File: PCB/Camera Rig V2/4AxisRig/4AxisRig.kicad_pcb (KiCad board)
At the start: 2 copper layers, 77 parts, among them J1 Conn_01x04_Socket, J2 SJ-3524-SMT, J3 Motor Connector, J4 Motor Connector, J5 USB_C_Receptacle_USB2.0_14P, J6 Motor Connector, Q1 NMOS, Q2 NMOS, U1 TPS25730DREFR, U4 ESP32-S3-WROOM-1, U5 TMC2209-LA, U6 TMC2209-LA, U7 TMC2209-LA

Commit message: PCB V2 first draft
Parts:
- added C1: 10uF, Capacitor_SMD:C_0603_1608Metric_Pad1.08x0.95mm_HandSolder, F.Cu at (131.9, 79.6)
- added C10: 10uF, Capacitor_SMD:C_0603_1608Metric_Pad1.08x0.95mm_HandSolder, F.Cu at (136.0, 67.7)
- added C11: 0.01uF, Capacitor_SMD:C_0603_1608Metric_Pad1.08x0.95mm_HandSolder, F.Cu at (132.8, 67.7)
- added C12: 330pF, Capacitor_SMD:C_0603_1608Metric_Pad1.08x0.95mm_HandSolder, F.Cu at (130.7, 73.0)
- added C13: 330pF, Capacitor_SMD:C_0603_1608Metric_Pad1.08x0.95mm_HandSolder, F.Cu at (130.7, 71.4)
- added C14: 10uF, Capacitor_SMD:C_0603_1608Metric_Pad1.08x0.95mm_HandSolder, F.Cu at (168.0, 76.1)
- added C15: 100nF, Capacitor_SMD:C_0603_1608Metric_Pad1.08x0.95mm_HandSolder, F.Cu at (164.3, 72.7)
- added C16: 47pF, Capacitor_SMD:C_0603_1608Metric_Pad1.08x0.95mm_HandSolder, F.Cu at (163.0, 80.5)
- added C17: 22uF, Capacitor_SMD:C_1206_3216Metric_Pad1.33x1.80mm_HandSolder, F.Cu at (159.2, 76.3)
- added C18: 22uF, Capacitor_SMD:C_1206_3216Metric_Pad1.33x1.80mm_HandSolder, F.Cu at (161.7, 76.3)
- added C19: 10uF, Capacitor_SMD:C_0603_1608Metric_Pad1.08x0.95mm_HandSolder, F.Cu at (155.4, 76.3)
- added C2: 10uF, Capacitor_SMD:C_0603_1608Metric_Pad1.08x0.95mm_HandSolder, F.Cu at (134.1, 78.6)
- added C20: 100nF, Capacitor_SMD:C_0603_1608Metric_Pad1.08x0.95mm_HandSolder, F.Cu at (151.9, 72.7)
- added C21: 47pF, Capacitor_SMD:C_0603_1608Metric_Pad1.08x0.95mm_HandSolder, F.Cu at (150.4, 80.6)
- added C22: 22uF, Capacitor_SMD:C_1206_3216Metric_Pad1.33x1.80mm_HandSolder, F.Cu at (149.1, 76.4)
- added C23: 22uF, Capacitor_SMD:C_1206_3216Metric_Pad1.33x1.80mm_HandSolder, F.Cu at (146.5, 76.4)
- added C24: 22uF, Capacitor_SMD:C_1206_3216Metric_Pad1.33x1.80mm_HandSolder, F.Cu at (85.4, 96.5)
- added C25: 1uF, Capacitor_SMD:C_0603_1608Metric_Pad1.08x0.95mm_HandSolder, F.Cu at (88.8, 97.0)
- added C26: 100nF, Capacitor_SMD:C_0603_1608Metric_Pad1.08x0.95mm_HandSolder, F.Cu at (84.6, 94.5)
- added C27: 100nF, Capacitor_SMD:C_0603_1608Metric_Pad1.08x0.95mm_HandSolder, F.Cu at (101.3, 64.6)
- added C28: 100nF, Capacitor_SMD:C_0603_1608Metric_Pad1.08x0.95mm_HandSolder, F.Cu at (88.8, 101.8)
- added C29: 100nF 16V, Capacitor_SMD:C_0603_1608Metric_Pad1.08x0.95mm_HandSolder, F.Cu at (167.0, 93.4)
- added C3: 4.7uF, Capacitor_SMD:C_0603_1608Metric_Pad1.08x0.95mm_HandSolder, F.Cu at (136.4, 78.6)
- added C30: 22nF 50V, Capacitor_SMD:C_0603_1608Metric_Pad1.08x0.95mm_HandSolder, F.Cu at (167.5, 95.0)
- added C31: 2.2uF 6.3V, Capacitor_SMD:C_0603_1608Metric_Pad1.08x0.95mm_HandSolder, F.Cu at (164.7, 90.5)
- added C32: 100nF, Capacitor_SMD:C_0603_1608Metric_Pad1.08x0.95mm_HandSolder, F.Cu at (165.5, 98.6)
- added C33: 100nF, Capacitor_SMD:C_0603_1608Metric_Pad1.08x0.95mm_HandSolder, F.Cu at (158.5, 98.6)
- added C34: 100uF, 865080545012:WCAP-ASLI_6.3X7.7_DXL_, F.Cu at (171.7, 89.4)
- added C35: 100nF, Capacitor_SMD:C_0603_1608Metric_Pad1.08x0.95mm_HandSolder, F.Cu at (156.9, 108.0)
- added C36: 100nF, Capacitor_SMD:C_0603_1608Metric_Pad1.08x0.95mm_HandSolder, F.Cu at (160.4, 108.0)
- added C37: 100nF, Capacitor_SMD:C_0603_1608Metric_Pad1.08x0.95mm_HandSolder, F.Cu at (164.0, 108.1)
- added C38: 100nF, Capacitor_SMD:C_0603_1608Metric_Pad1.08x0.95mm_HandSolder, F.Cu at (167.6, 108.1)
- added C39: 100nF 16V, Capacitor_SMD:C_0603_1608Metric_Pad1.08x0.95mm_HandSolder, F.Cu at (150.0, 93.3)
- added C4: 4.7uF, Capacitor_SMD:C_0603_1608Metric_Pad1.08x0.95mm_HandSolder, F.Cu at (131.2, 67.7)
- added C40: 22nF 50V, Capacitor_SMD:C_0603_1608Metric_Pad1.08x0.95mm_HandSolder, F.Cu at (150.5, 94.9)
- added C41: 2.2uF 6.3V, Capacitor_SMD:C_0603_1608Metric_Pad1.08x0.95mm_HandSolder, F.Cu at (147.7, 90.5)
- added C42: 100nF, Capacitor_SMD:C_0603_1608Metric_Pad1.08x0.95mm_HandSolder, F.Cu at (148.5, 98.6)
- added C43: 100nF, Capacitor_SMD:C_0603_1608Metric_Pad1.08x0.95mm_HandSolder, F.Cu at (141.5, 98.6)
- added C44: 100uF, 865080545012:WCAP-ASLI_6.3X7.7_DXL_, F.Cu at (154.7, 89.4)
- added C45: 100nF, Capacitor_SMD:C_0603_1608Metric_Pad1.08x0.95mm_HandSolder, F.Cu at (139.9, 108.0)
- added C46: 100nF, Capacitor_SMD:C_0603_1608Metric_Pad1.08x0.95mm_HandSolder, F.Cu at (143.4, 108.0)
- added C47: 100nF, Capacitor_SMD:C_0603_1608Metric_Pad1.08x0.95mm_HandSolder, F.Cu at (147.0, 108.0)
- added C48: 100nF, Capacitor_SMD:C_0603_1608Metric_Pad1.08x0.95mm_HandSolder, F.Cu at (150.6, 108.0)
- added C49: 100nF 16V, Capacitor_SMD:C_0603_1608Metric_Pad1.08x0.95mm_HandSolder, F.Cu at (133.0, 93.3)
- added C5: 0.01uF, Capacitor_SMD:C_0603_1608Metric_Pad1.08x0.95mm_HandSolder, F.Cu at (130.7, 76.2)
- added C50: 22nF 50V, Capacitor_SMD:C_0603_1608Metric_Pad1.08x0.95mm_HandSolder, F.Cu at (133.5, 94.9)
- added C51: 2.2uF 6.3V, Capacitor_SMD:C_0603_1608Metric_Pad1.08x0.95mm_HandSolder, F.Cu at (130.7, 90.5)
- added C52: 100nF, Capacitor_SMD:C_0603_1608Metric_Pad1.08x0.95mm_HandSolder, F.Cu at (131.5, 98.6)
- added C53: 100nF, Capacitor_SMD:C_0603_1608Metric_Pad1.08x0.95mm_HandSolder, F.Cu at (124.5, 98.6)
- added C54: 100uF, 865080545012:WCAP-ASLI_6.3X7.7_DXL_, F.Cu at (137.7, 89.5)
- added C55: 100nF, Capacitor_SMD:C_0603_1608Metric_Pad1.08x0.95mm_HandSolder, F.Cu at (122.5, 108.0)
- added C56: 100nF, Capacitor_SMD:C_0603_1608Metric_Pad1.08x0.95mm_HandSolder, F.Cu at (126.4, 108.0)
- added C57: 100nF, Capacitor_SMD:C_0603_1608Metric_Pad1.08x0.95mm_HandSolder, F.Cu at (130.0, 108.0)
- added C58: 100nF, Capacitor_SMD:C_0603_1608Metric_Pad1.08x0.95mm_HandSolder, F.Cu at (133.6, 108.0)
- added C6: 0.01uF, Capacitor_SMD:C_0603_1608Metric_Pad1.08x0.95mm_HandSolder, F.Cu at (130.7, 74.6)
- added C7: 22uF, Capacitor_SMD:C_1206_3216Metric_Pad1.33x1.80mm_HandSolder, F.Cu at (138.1, 66.9)
- added C8: 22uF, Capacitor_SMD:C_1206_3216Metric_Pad1.33x1.80mm_HandSolder, F.Cu at (140.7, 66.9)
- added C9: 0.01uF, Capacitor_SMD:C_0603_1608Metric_Pad1.08x0.95mm_HandSolder, F.Cu at (134.4, 67.7)
- added D1: ESD441, Diode_SMD:D_0402_1005Metric_Pad0.77x0.64mm_HandSolder, F.Cu at (115.9, 72.0)
- added D2: ESD441, Diode_SMD:D_0402_1005Metric_Pad0.77x0.64mm_HandSolder, F.Cu at (118.1, 72.0)
- added D3: ESD441, Diode_SMD:D_0402_1005Metric_Pad0.77x0.64mm_HandSolder, F.Cu at (119.4, 72.0)
- added D4: ESD441, Diode_SMD:D_0402_1005Metric_Pad0.77x0.64mm_HandSolder, F.Cu at (114.7, 72.0)
- added D5: SMAJ10CA-13-F, SMAJ10CA-13-F:SMA_DIO, F.Cu at (124.0, 70.2)
- added FB13: 2512065007Y6, Inductor_SMD:L_1206_3216Metric_Pad1.22x1.90mm_HandSolder, F.Cu at (85.4, 99.0)
- added H1: MountingHole, MountingHole:MountingHole_3.2mm_M3, F.Cu at (173.0, 66.0)
- added H2: MountingHole, MountingHole:MountingHole_3.2mm_M3, F.Cu at (173.0, 113.0)
- added H3: MountingHole, MountingHole:MountingHole_3.2mm_M3, F.Cu at (86.0, 66.0)
- added H4: MountingHole, MountingHole:MountingHole_3.2mm_M3, F.Cu at (86.0, 113.0)
- added L1: 4.7uH, DR74-4R7-R:DR74, F.Cu at (160.4, 67.5)
- added L2: 15uH, DR74-150-R:DR74, F.Cu at (149.4, 67.6)
- added R45: 4.7k, Resistor_SMD:R_0603_1608Metric_Pad0.98x0.95mm_HandSolder, F.Cu at (88.3, 70.4)
- added R46: 10k, Resistor_SMD:R_0603_1608Metric_Pad0.98x0.95mm_HandSolder, F.Cu at (90.5, 101.8)
- added SW1: PTS810SJS250SMTRLFS, PTS810SJS250SMTR:SMT_MTRLFS_CNK, F.Cu at (105.7, 64.5)
- added SW2: SW_SPDT, SS-12D07-VG 4 NS GA PA:SS12D07_CNK, F.Cu at (107.8, 69.6)
- added SW3: PEC11L-4120F-S0020, PEC11L-4120F-S0020:PEC11L-4x20F-Sxxx_BRN, F.Cu at (101.9, 100.4)
- added TP1: TestPoint, TestPoint:TestPoint_Pad_2.0x2.0mm, F.Cu at (131.5, 83.5)
- FB1, FB10, FB11, FB12, FB2, FB3, FB4, FB5, FB6, FB7, FB8, FB9: value 50@100MHz -> 2512065007Y6
- J1: value Conn_01x04_Socket -> Conn_01x05_Socket
- J5: value USB_C_Receptacle_USB2.0_14P -> USB_C_Receptacle_USB2.0_16P; footprint USB_GCT:CONN_8p94X6p5X3p16_12L_GCC -> USB_C_Receptacle_USB2.0_14P:CONN_8p94X6p5X3p16_12L_GCC
- Q1, Q2: footprint 2N7002KT7G:SOT95P240X111-3N -> 2N7000:SOT95P240X111-3N
- R19: value 10k -> 100k
- R20: value 10k -> 25k
- R21, R22: value 500 -> 10k
- R27, R33, R41: value 220m -> 10k
- R28, R34, R42: value 220m -> 0.68; footprint Resistor_SMD:R_0603_1608Metric_Pad0.98x0.95mm_HandSolder -> Resistor_SMD:R_1206_3216Metric_Pad1.30x1.75mm_HandSolder
- R29: value 10k -> 0.68; footprint Resistor_SMD:R_0603_1608Metric_Pad0.98x0.95mm_HandSolder -> Resistor_SMD:R_1206_3216Metric_Pad1.30x1.75mm_HandSolder
- R35: value 5.1k -> 0.68; footprint Resistor_SMD:R_0603_1608Metric_Pad0.98x0.95mm_HandSolder -> Resistor_SMD:R_1206_3216Metric_Pad1.30x1.75mm_HandSolder
- R36: value 5.1k -> 5.1k+-10%
- R37: value 10k -> 5.1k+-10%
- R43: value 100k -> 0.68; footprint Resistor_SMD:R_0603_1608Metric_Pad0.98x0.95mm_HandSolder -> Resistor_SMD:R_1206_3216Metric_Pad1.30x1.75mm_HandSolder
- R44: value 25k -> 4.7k
- RV1, RV2, RV3, RV4, RV5, RV6: footprint Resistor_SMD:R_0603_1608Metric_Pad0.98x0.95mm_HandSolder -> Resistor_SMD:R_1206_3216Metric_Pad1.30x1.75mm_HandSolder
- U2, U3: value ~ -> AN_SY8105
- moved J1 104.7 mm to (94.4, 65.5)
- moved R1 91.4 mm to (95.5, 94.4)
- moved J5 74.9 mm to (117.0, 64.9), turned to 180 degrees
- moved R36 69.2 mm to (120.7, 72.5), turned to -90 degrees
- moved J4 61.5 mm to (149.0, 113.5), turned to -90 degrees
- moved FB5 55.0 mm to (141.3, 104.5), turned to -90 degrees
- moved J6 53.6 mm to (132.0, 113.5), turned to -90 degrees
- moved FB6 50.7 mm to (143.9, 104.5), turned to -90 degrees
- moved FB9 50.6 mm to (124.3, 104.5), turned to -90 degrees
- moved U1 50.4 mm to (135.2, 73.2), turned to 90 degrees
- moved R34 49.7 mm to (124.6, 100.6)
- moved R29 49.4 mm to (141.6, 100.6)
- moved R37 49.3 mm to (113.4, 72.5), turned to -90 degrees
- moved R5 49.2 mm to (128.0, 72.4), turned to -90 degrees
- moved FB10 46.7 mm to (126.9, 104.5), turned to -90 degrees
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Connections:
- net /D+ renamed /USB_D+
- net /D- renamed /USB_D-
- FB1 pad 1: /TMC2209 1/OA1 -> /TMC2209 1/OA2
- FB10 pad 1: /TMC2209 3/OA2 -> /TMC2209 3/OA1
- FB2 pad 1: /TMC2209 1/OA2 -> /TMC2209 1/OA1
- FB5 pad 1: /TMC2209 2/OA1 -> /TMC2209 2/OA2
- FB6 pad 1: /TMC2209 2/OA2 -> /TMC2209 2/OA1
- FB9 pad 1: /TMC2209 3/OA1 -> /TMC2209 3/OA2
- J1 pad MP: (no net) -> unconnected-(J1-Pin_5-PadMP)_1
- J5 pad A5: /USB Power/CC1 -> /USB_CC1
- J5 pad A8: (no net) -> unconnected-(J5-SBU1-PadA8)
- J5 pad B5: /USB Power/CC2 -> /USB_CC2
- J5 pad B8: (no net) -> unconnected-(J5-SBU2-PadB8)
- R19 pad 1: /EN -> Net-(U4-IO41)
- R19 pad 2: +3V3 -> /PPHV
- R20 pad 1: /MCU ESP32/BOOT -> GND
- R20 pad 2: +3V3 -> Net-(U4-IO41)
- R21 pad 1: /SHUTTER -> /MCU ESP32/EN
- R21 pad 2: Net-(Q1-G) -> +3V3
- R22 pad 1: /FOCUS -> /SHUTTER
- R22 pad 2: Net-(Q2-G) -> Net-(Q1-G)
- R23 pad 1: GND -> /FOCUS
- R23 pad 2: /TMC2209 1/AD0 -> Net-(Q2-G)
- R24 pad 1: /TMC2209 1/AD0 -> GND
- R24 pad 2: +3V3 -> /TMC2209 1/AD0
- R25 pad 1: GND -> /TMC2209 1/AD0
- R25 pad 2: /TMC2209 1/AD1 -> +3V3
- R26 pad 1: /TMC2209 1/AD1 -> GND
- R26 pad 2: +3V3 -> /TMC2209 1/AD1
- R27 pad 1: GND -> /TMC2209 1/AD1
- R27 pad 2: Net-(U5-BRB) -> +3V3
- R29 pad 2: /TMC2209 2/AD0 -> Net-(U6-BRA)
- R30 pad 1: /TMC2209 2/AD0 -> GND
- R30 pad 2: +3V3 -> /TMC2209 2/AD0
- R31 pad 1: GND -> /TMC2209 2/AD0
- R31 pad 2: /TMC2209 2/AD1 -> +3V3
- R32 pad 1: /TMC2209 2/AD1 -> GND
- R32 pad 2: +3V3 -> /TMC2209 2/AD1
- R33 pad 1: GND -> /TMC2209 2/AD1
- R33 pad 2: Net-(U6-BRB) -> +3V3
- R34 pad 2: Net-(U6-BRA) -> Net-(U7-BRA)
- R35 pad 1: /USB Power/CC1 -> GND
- R35 pad 2: GND -> Net-(U5-BRB)
- R36 pad 1: /USB Power/CC2 -> /USB_CC1
- R37 pad 1: GND -> /USB_CC2
- R37 pad 2: /TMC2209 3/AD0 -> GND
- R38 pad 1: /TMC2209 3/AD0 -> GND
- R38 pad 2: +3V3 -> /TMC2209 3/AD0
- R39 pad 1: GND -> /TMC2209 3/AD0
- R39 pad 2: /TMC2209 3/AD1 -> +3V3
- R40 pad 1: /TMC2209 3/AD1 -> GND
- R40 pad 2: +3V3 -> /TMC2209 3/AD1
- R41 pad 1: GND -> /TMC2209 3/AD1
- R41 pad 2: Net-(U7-BRB) -> +3V3
- R42 pad 2: Net-(U7-BRA) -> Net-(U6-BRB)
- R43 pad 1: Net-(U4-IO3) -> GND
- R43 pad 2: /PPHV -> Net-(U7-BRB)
- R44 pad 1: GND -> /I2C_SCL
- R44 pad 2: Net-(U4-IO3) -> +3V3
- U1 pad 20: /Buck Converter 12V/VIN -> /PPHV
- U1 pad 21: /Buck Converter 12V/VIN -> /PPHV
- U1 pad 22: /Buck Converter 12V/VIN -> /PPHV
- U1 pad 28: /USB Power/CC1 -> /USB_CC1
- U1 pad 29: /USB Power/CC2 -> /USB_CC2
- U2 pad 4: /Buck Converter 12V/VIN -> /PPHV
- U3 pad 4: /Buck Converter 12V/VIN -> /PPHV
- U4 pad 12: /STEP2 -> unconnected-(U4-IO8-Pad12)
- U4 pad 15: Net-(U4-IO3) -> /SPREAD
- U4 pad 16: /ENC_C -> /EN_DRIVERS
- U4 pad 17: /DIR2 -> /STDBY3
- U4 pad 18: /DIAG2 -> /DIR3
- U4 pad 19: /STDBY2 -> /STEP3
- U4 pad 2: +3V3 -> Net-(U4-3V3)
- U4 pad 20: /STEP3 -> /DIAG3
- U4 pad 21: /DIR3 -> /STDBY2
- U4 pad 22: /DIAG3 -> /DIR2
- U4 pad 23: unconnected-(U4-IO21-Pad23) -> /STEP2
- U4 pad 24: /ENC_B -> /DIAG2
- U4 pad 25: /SPREAD -> /STDBY1
- U4 pad 26: /ENC_A -> /DIR1
- U4 pad 28: unconnected-(U4-IO35-Pad28) -> /STEP1
- U4 pad 29: unconnected-(U4-IO36-Pad29) -> /DIAG1
- U4 pad 3: /EN -> /MCU ESP32/EN
- U4 pad 32: /EN_12V -> unconnected-(U4-IO39-Pad32)
- U4 pad 33: /SW -> /EN_12V
- U4 pad 34: /SHUTTER -> Net-(U4-IO41)
- U4 pad 35: /FOCUS -> unconnected-(U4-IO42-Pad35)
- U4 pad 4: /STEP1 -> /SW
- U4 pad 5: /DIR1 -> /ENC_B
- U4 pad 6: /DIAG1 -> /ENC_C
- U4 pad 7: /STDBY1 -> /ENC_A
- U4 pad 8: /STDBY3 -> /SHUTTER
- U4 pad 9: /EN -> /FOCUS
- U5 pad 2: /EN -> /EN_DRIVERS
- U6 pad 2: /EN -> /EN_DRIVERS
- U7 pad 2: /EN -> /EN_DRIVERS
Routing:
- net /SPREAD: track 0.00 -> 171.6 mm, vias 0 -> 4
- net GND: track 0.00 -> 156.0 mm, vias 0 -> 95
- net /EN_DRIVERS: track 0.00 -> 154.9 mm, vias 0 -> 4
- net /UART_TX/RX: track 0.00 -> 87.4 mm, vias 0 -> 4
- net /EN_12V: track 0.00 -> 83.0 mm, vias 0 -> 4
- net /DIAG1: track 0.00 -> 73.6 mm, vias 0 -> 2
- net /STEP1: track 0.00 -> 69.7 mm, vias 0 -> 2
- net /DIR1: track 0.00 -> 65.9 mm, vias 0 -> 2
- net /STDBY1: track 0.00 -> 65.6 mm, vias 0 -> 2
- net +3V3: track 0.00 -> 57.8 mm, vias 0 -> 24
- net /PPHV: track 0.00 -> 55.8 mm, vias 0 -> 36
- net /USB_D-: track 0.00 -> 52.0 mm
- net /USB_D+: track 0.00 -> 49.9 mm
- net /DIAG2: track 0.00 -> 49.5 mm, vias 0 -> 2
- net /MCU ESP32/EN: track 0.00 -> 48.4 mm, vias 0 -> 2
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- added copper zone on F.Cu, net +12V
- added copper zone on In2.Cu, net +12V
- added copper zone on F.Cu, net +3V3
- added copper zone on In2.Cu, net +3V3
- added copper zone on F.Cu, net /PPHV
- added copper zone on In2.Cu, net /PPHV
- added copper zone on F.Cu, net /USB Power/VBUS
- added copper zone on In2.Cu, net /USB Power/VBUS
- added copper zone on B.Cu, net GND
- added copper zone on F.Cu, net GND
- added copper zone on In1.Cu, net GND
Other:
- board outline added: 95 x 55 mm
- copper layers 2 -> 4
- board text added: "Camera Motion Driver V2 Andrew Josephbek"

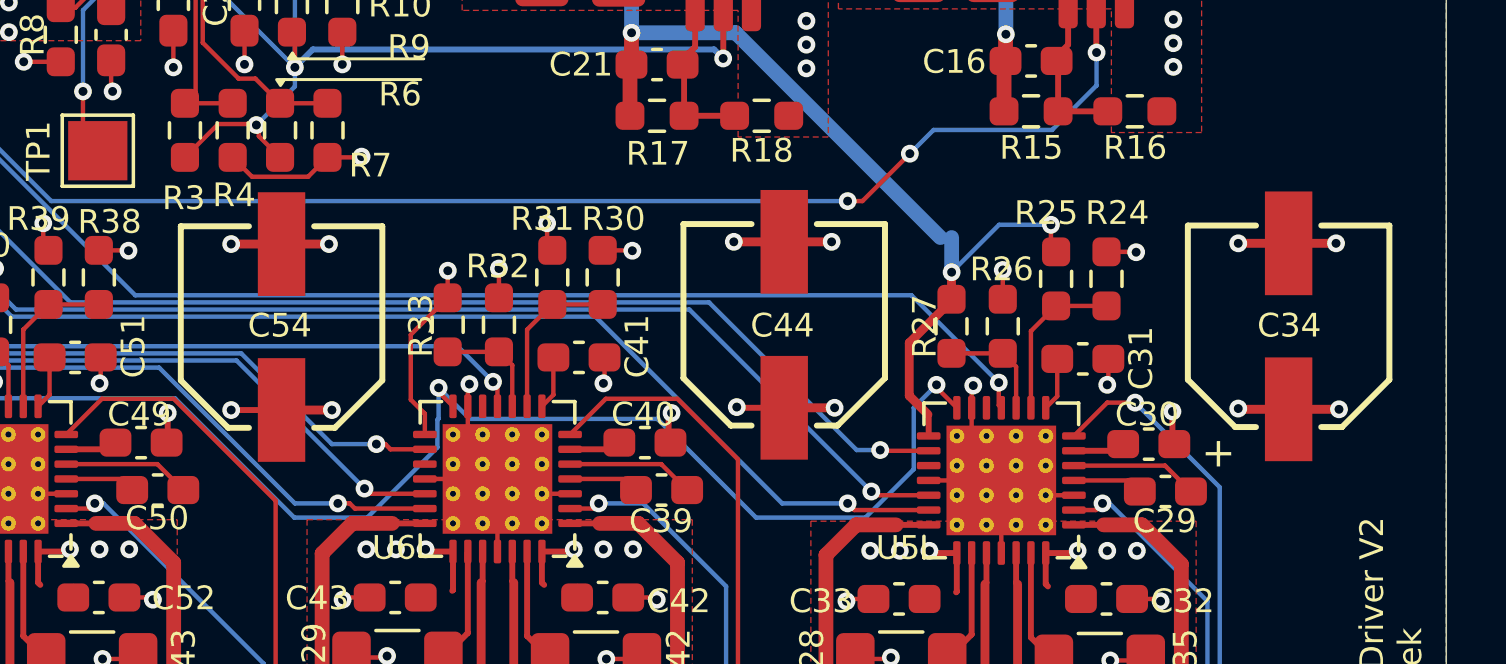
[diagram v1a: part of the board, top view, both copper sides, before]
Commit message: REplaced bulk caps w low esr ceramics
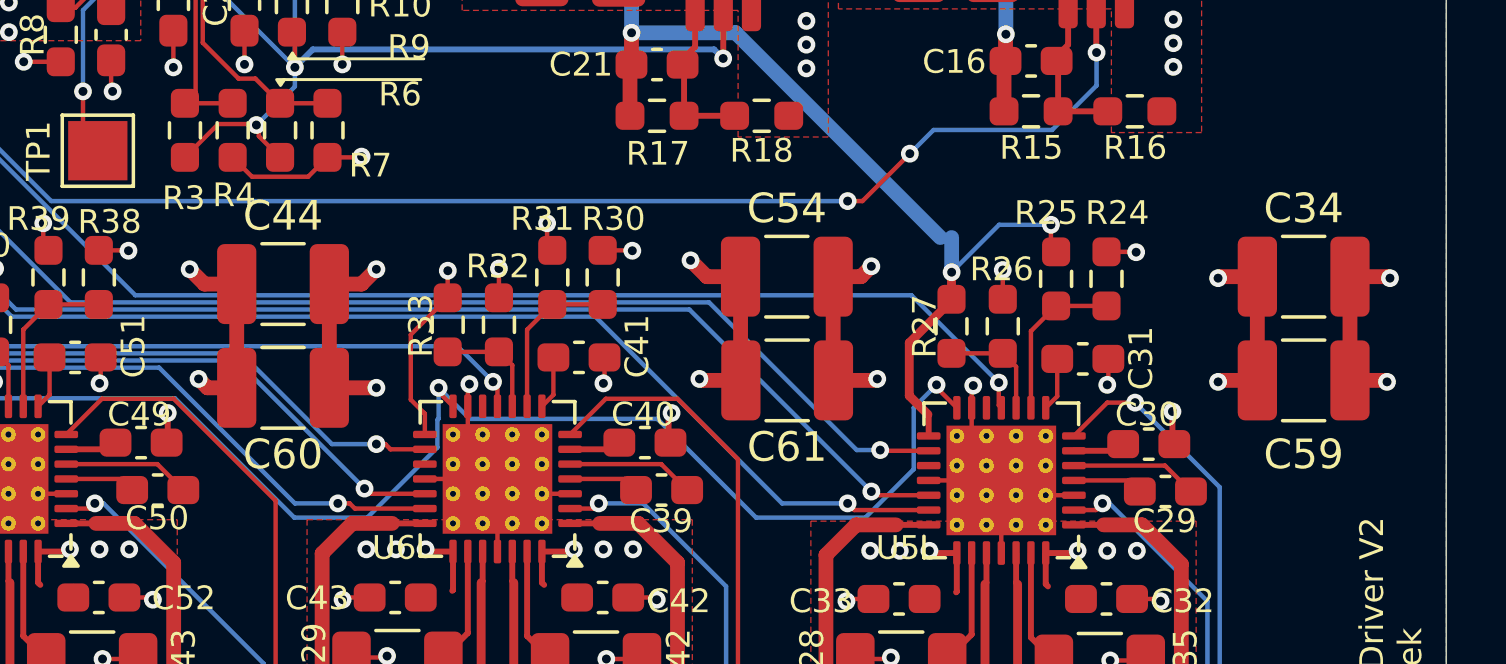
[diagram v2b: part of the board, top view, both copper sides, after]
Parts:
- added C59: 47uF, Capacitor_SMD:C_1210_3225Metric_Pad1.33x2.70mm_HandSolder, F.Cu at (172.2, 91.2)
- added C60: 47uF, Capacitor_SMD:C_1210_3225Metric_Pad1.33x2.70mm_HandSolder, F.Cu at (137.8, 91.5)
- added C61: 47uF, Capacitor_SMD:C_1210_3225Metric_Pad1.33x2.70mm_HandSolder, F.Cu at (154.8, 91.2)
- C34, C44, C54: value 100uF -> 47uF; footprint 865080545012:WCAP-ASLI_6.3X7.7_DXL_ -> Capacitor_SMD:C_1210_3225Metric_Pad1.33x2.70mm_HandSolder
- moved C54 17.1 mm to (154.8, 87.8), turned to 0 degrees
- moved C44 17.0 mm to (137.8, 88.0), turned to 0 degrees
- moved C34 1.75 mm to (172.2, 87.8), turned to 0 degrees
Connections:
- C34 pad 1: +12V -> GND
- C34 pad 2: GND -> +12V
- C44 pad 1: +12V -> GND
- C44 pad 2: GND -> +12V
- C54 pad 1: +12V -> GND
- C54 pad 2: GND -> +12V
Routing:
- net GND: track 156.0 -> 165.9 mm
- net +12V: track 37.6 -> 47.0 mm

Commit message: Updated rotary encoder wiring
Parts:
- added C62: 100nF, Capacitor_SMD:C_0603_1608Metric_Pad1.08x0.95mm_HandSolder, F.Cu at (96.7, 98.4)
- added C63: 100nF, Capacitor_SMD:C_0603_1608Metric_Pad1.08x0.95mm_HandSolder, F.Cu at (96.7, 96.8)
- added R47: 10k, Resistor_SMD:R_0603_1608Metric_Pad0.98x0.95mm_HandSolder, F.Cu at (89.6, 104.8)
- added R48: 10k, Resistor_SMD:R_0603_1608Metric_Pad0.98x0.95mm_HandSolder, F.Cu at (89.6, 106.4)
- added R49: 10k, Resistor_SMD:R_0603_1608Metric_Pad0.98x0.95mm_HandSolder, F.Cu at (93.2, 98.4)
- added R50: 10k, Resistor_SMD:R_0603_1608Metric_Pad0.98x0.95mm_HandSolder, F.Cu at (93.2, 96.8)
- moved SW3 0.40 mm to (101.9, 100.8)
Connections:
- SW3 pad A: /ENC_A -> Net-(R48-Pad2)
- SW3 pad B: /ENC_B -> Net-(R47-Pad2)
- SW3 pad C: /ENC_C -> GND
- U4 pad 6: /ENC_C -> /ENC_A
- U4 pad 7: /ENC_A -> unconnected-(U4-IO7-Pad7)
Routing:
- net Net-(R48-Pad2): track 0.00 -> 25.4 mm, vias 0 -> 1
- net Net-(R47-Pad2): track 0.00 -> 15.5 mm, vias 0 -> 1
- net /ENC_C: track 13.0 -> 0.00 mm
- net /ENC_A: track 14.7 -> 7.93 mm
- net +12V: track 47.0 -> 42.4 mm, vias 37 -> 34
- net GND: track 165.9 -> 169.1 mm
- net +3V3: track 57.8 -> 60.6 mm, vias 24 -> 25
- net /ENC_B: track 11.8 -> 10.4 mm

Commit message: Updated figs
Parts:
- added D6: SMAJ10CA-13-F, SMAJ10CA-13-F:SMA_DIO, F.Cu at (172.8, 78.0)
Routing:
- net +12V: track 42.4 -> 44.3 mm, vias 34 -> 35
- net GND: track 169.1 -> 170.9 mm, vias 95 -> 96

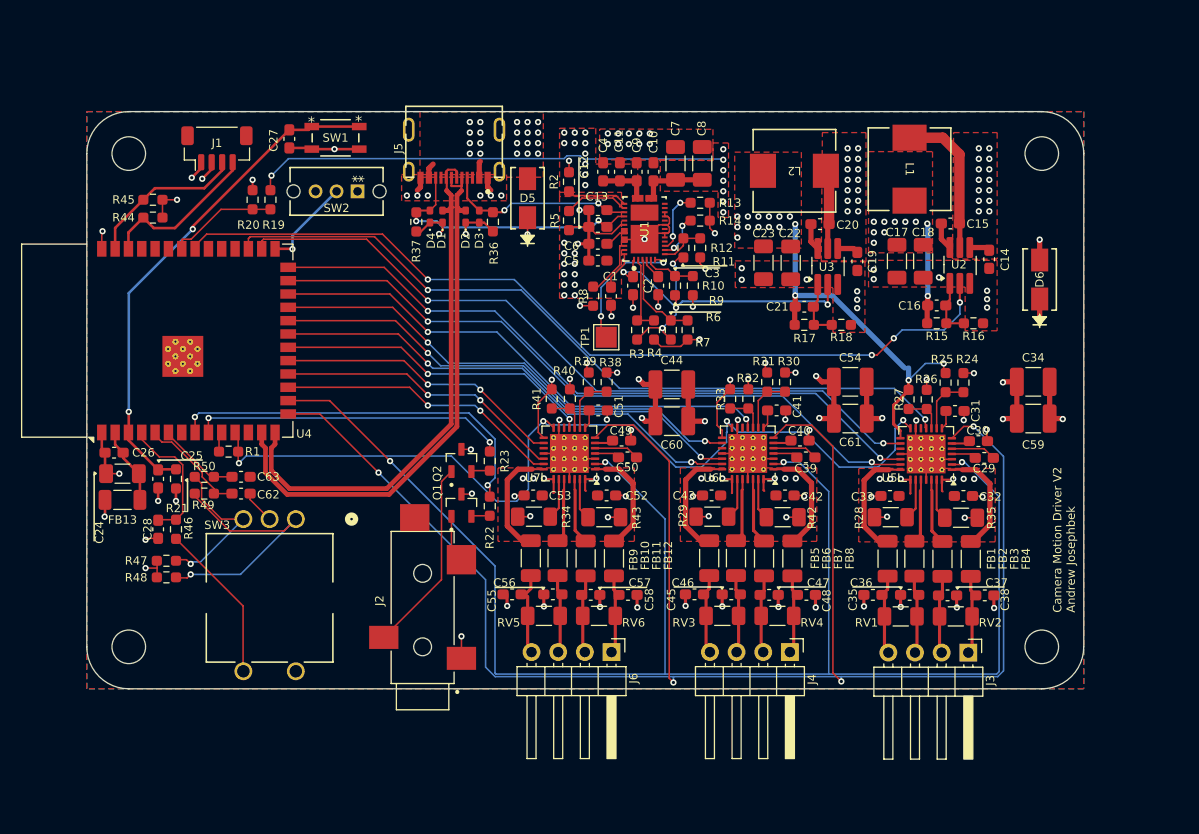
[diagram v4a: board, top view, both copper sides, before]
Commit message: Netclass Improvements
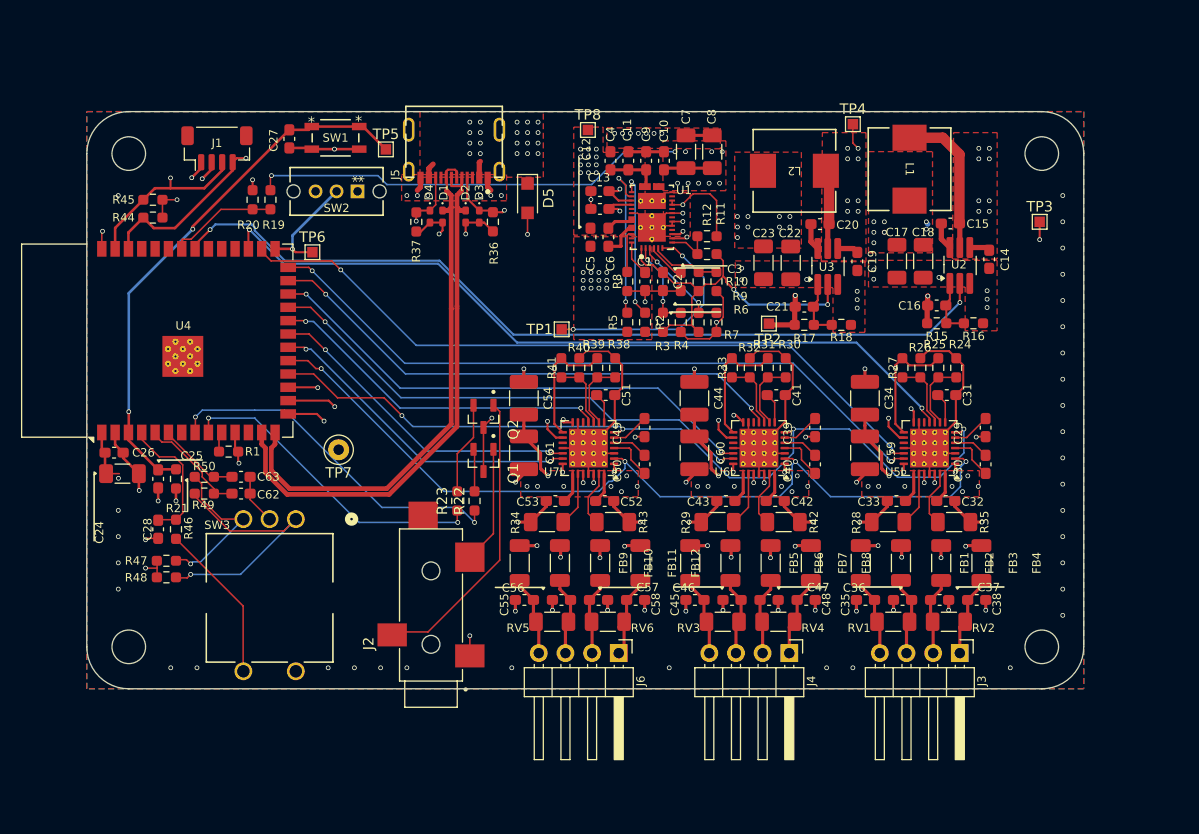
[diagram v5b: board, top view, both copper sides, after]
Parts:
- removed D6: SMAJ10CA-13-F, SMAJ10CA-13-F:SMA_DIO
- removed FB13: 2512065007Y6, Inductor_SMD:L_1206_3216Metric_Pad1.22x1.90mm_HandSolder
- removed R13, R14: 10k, Resistor_SMD:R_0603_1608Metric_Pad0.98x0.95mm_HandSolder
- added TP2: TestPoint, TestPoint:TestPoint_Pad_1.0x1.0mm, F.Cu at (147.0, 82.2)
- added TP3: TestPoint, TestPoint:TestPoint_Pad_1.0x1.0mm, F.Cu at (172.8, 72.5)
- added TP4: TestPoint, TestPoint:TestPoint_Pad_1.0x1.0mm, F.Cu at (155.0, 63.2)
- added TP5: TestPoint, TestPoint:TestPoint_Pad_1.0x1.0mm, F.Cu at (110.5, 65.6)
- added TP6: TestPoint, TestPoint:TestPoint_Pad_1.0x1.0mm, F.Cu at (103.5, 75.4)
- added TP7: TestPoint, TestPoint:TestPoint_Keystone_5000-5004_Miniature, F.Cu at (106.0, 94.2)
- added TP8: TestPoint, TestPoint:TestPoint_Pad_1.0x1.0mm, F.Cu at (129.8, 63.8)
- D5: value SMAJ10CA-13-F -> T4F10A; footprint SMAJ10CA-13-F:SMA_DIO -> Diode_SMD:Nexperia_CFP3_SOD-123W
- R20: value 25k -> 19k
- RV1, RV2, RV3, RV4, RV5, RV6: value >12 VDC -> CG0603MLA-18KE
- TP1: footprint TestPoint:TestPoint_Pad_2.0x2.0mm -> TestPoint:TestPoint_Pad_1.0x1.0mm
- moved C61 31.3 mm to (123.7, 94.5), turned to 90 degrees
- moved C54 31.1 mm to (123.7, 89.3), turned to -90 degrees
- moved C59 16.4 mm to (156.2, 94.5), turned to 90 degrees
- moved C34 16.1 mm to (156.2, 89.3), turned to -90 degrees
- moved R2 15.2 mm to (135.2, 82.1), turned to -90 degrees
- moved R5 11.2 mm to (133.5, 82.1)
- moved R23 4.90 mm to (117.3, 99.1), turned to 90 degrees
- moved Q1 4.76 mm to (119.8, 95.2), turned to -90 degrees
- moved Q2 4.70 mm to (119.8, 91.0), turned to -90 degrees
- moved TP1 4.32 mm to (127.2, 82.8)
- moved C60 3.70 mm to (139.9, 94.5), turned to 90 degrees
- moved C1 3.54 mm to (135.2, 78.2)
- moved R8 3.54 mm to (133.5, 78.2)
- moved R41 3.10 mm to (127.2, 86.4)
- moved R40 3.09 mm to (128.9, 86.4)
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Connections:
- net +12V renamed /12V
- C11 pad 1: /USB Power/VBUS -> /VBUS
- C21 pad 1: +3V3 -> /3V3
- C22 pad 1: +3V3 -> /3V3
- C23 pad 1: +3V3 -> /3V3
- C24 pad 1: Net-(U4-3V3) -> /3V3
- C26 pad 1: Net-(U4-3V3) -> /3V3
- C4 pad 1: /USB Power/VBUS -> /VBUS
- C5 pad 1: /USB Power/VBUS -> /VBUS
- C6 pad 1: /USB Power/VBUS -> /VBUS
- C9 pad 1: /USB Power/VBUS -> /VBUS
- D1 pad 1: GND -> /USB_D+
- D1 pad 2: /USB_D+ -> GND
- D2 pad 1: GND -> /USB_D-
- D2 pad 2: /USB_D- -> GND
- D3 pad 1: GND -> /USB_CC1
- D3 pad 2: /USB_CC1 -> GND
- D4 pad 1: GND -> /USB_CC2
- D4 pad 2: /USB_CC2 -> GND
- D5 pad 1: GND -> /VBUS
- D5 pad 2: /USB Power/VBUS -> GND
- J1 pad 2: +3V3 -> /3V3
- J5 pad A4: /USB Power/VBUS -> /VBUS
- J5 pad A9: /USB Power/VBUS -> /VBUS
- J5 pad B4: /USB Power/VBUS -> /VBUS
- J5 pad B9: /USB Power/VBUS -> /VBUS
- L2 pad 2: +3V3 -> /3V3
- R17 pad 1: +3V3 -> /3V3
- R21 pad 2: +3V3 -> /3V3
- R25 pad 2: +3V3 -> /3V3
- R27 pad 2: +3V3 -> /3V3
- R31 pad 2: +3V3 -> /3V3
- R33 pad 2: +3V3 -> /3V3
- R39 pad 2: +3V3 -> /3V3
- R41 pad 2: +3V3 -> /3V3
- R44 pad 2: +3V3 -> /3V3
- R45 pad 2: +3V3 -> /3V3
- R47 pad 1: +3V3 -> /3V3
- R48 pad 1: +3V3 -> /3V3
- SW2 pad 1: +3V3 -> /3V3
- U1 pad 23: /USB Power/VBUS -> /VBUS
- U1 pad 24: /USB Power/VBUS -> /VBUS
- U1 pad 25: /USB Power/VBUS -> /VBUS
- U1 pad 32: /USB Power/VBUS -> /VBUS
- U1 pad 33: /USB Power/VBUS -> /VBUS
- U1 pad 8: Net-(U1-I2Ct_SDA) -> /I2C_SDA
- U1 pad 9: Net-(U1-I2Ct_SCL) -> /I2C_SCL
- U4 pad 15: /SPREAD -> /STEP3
- U4 pad 16: /EN_DRIVERS -> /STEP2
- U4 pad 17: /STDBY3 -> /STEP1
- U4 pad 18: /DIR3 -> /SPREAD
- U4 pad 19: /STEP3 -> /EN_DRIVERS
- U4 pad 2: Net-(U4-3V3) -> /3V3
- U4 pad 20: /DIAG3 -> /STDBY3
- U4 pad 21: /STDBY2 -> /DIR3
- U4 pad 22: /DIR2 -> /DIAG3
- U4 pad 23: /STEP2 -> /STDBY2
- U4 pad 24: /DIAG2 -> /DIR2
- U4 pad 25: /STDBY1 -> /DIAG2
- U4 pad 26: /DIR1 -> /STDBY1
- U4 pad 28: /STEP1 -> /DIR1
- U5 pad 15: +3V3 -> /3V3
- U6 pad 15: +3V3 -> /3V3
- U7 pad 15: +3V3 -> /3V3
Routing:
- net /SPREAD: track 171.6 -> 79.8 mm
- net /EN_DRIVERS: track 154.9 -> 82.5 mm
- net +3V3: track 60.6 -> 0.00 mm, vias 25 -> 0
- net /3V3: track 0.00 -> 56.2 mm, vias 0 -> 18
- net /I2C_SDA: track 15.2 -> 70.5 mm, vias 0 -> 2
- net /I2C_SCL: track 15.5 -> 63.5 mm, vias 0 -> 2
- net GND: track 170.9 -> 203.8 mm, vias 96 -> 112
- net /VBUS: track 0.00 -> 10.6 mm, vias 0 -> 32
- net /USB Power/VBUS: track 10.1 -> 0.00 mm, vias 41 -> 0
- net /Shutter Control/CAM_FOCUS: track 18.5 -> 28.2 mm
- net /USB Power/CAP_MIS: track 12.8 -> 22.2 mm
- net /USB Power/RES_27: track 6.28 -> 15.6 mm, vias 0 -> 2
- net /STEP1: track 69.7 -> 61.4 mm
- net /USB Power/RES_26: track 5.77 -> 14.0 mm, vias 0 -> 2
- net Net-(U4-3V3): track 7.40 -> 0.00 mm
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- added copper zone on F.Cu, net /3V3
- added copper zone on In2.Cu, net /3V3
- added copper zone on F.Cu, net /VBUS
- added copper zone on In2.Cu, net /VBUS
- removed copper zone on F.Cu, net +3V3
- removed copper zone on In2.Cu, net +3V3
- removed copper zone on F.Cu, net /USB Power/VBUS
- removed copper zone on In2.Cu, net /USB Power/VBUS
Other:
- board text removed: "Camera Motion Driver V2 Andrew Josephbek"
